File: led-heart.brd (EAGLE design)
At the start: 55 x 44.9 mm, 65 parts, among them IC1 FT232RL, IC2 MSP430F149, Q1 8mhz, T1 MMBT3904, T2 MMBT3904, X1 USB_MINI-B

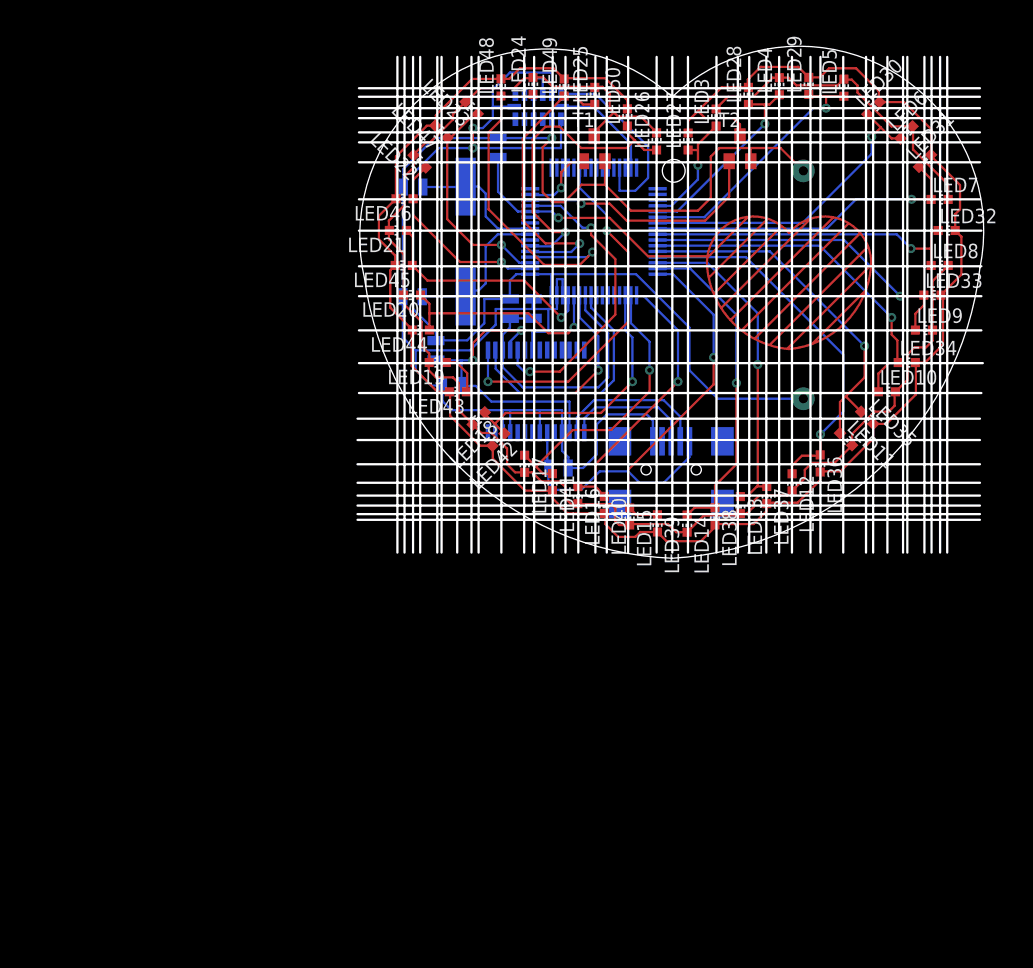
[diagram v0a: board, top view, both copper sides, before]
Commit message: release, fix schematic, pcb, silk, docs
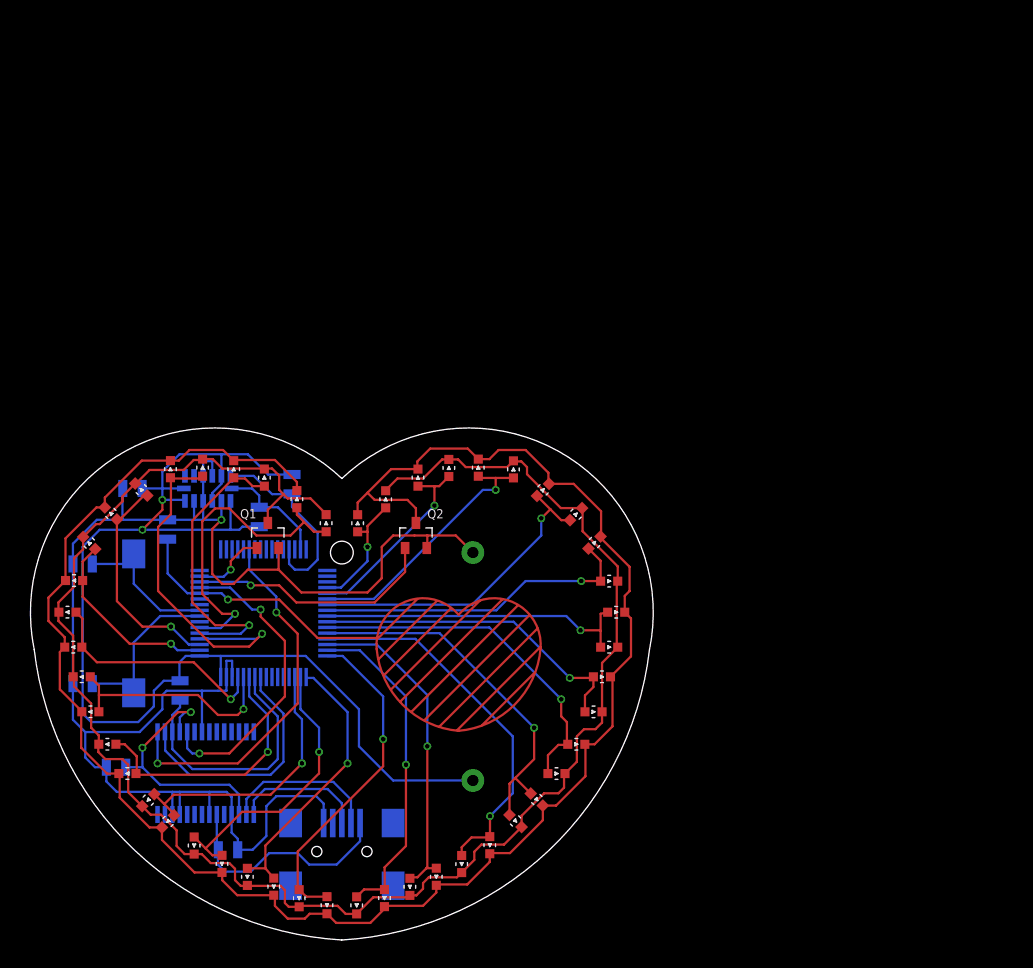
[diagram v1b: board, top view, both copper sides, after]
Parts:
- removed D1: LIS302DL, colibri:LGA14
- removed R5: 100k, colibri:R0805
- removed T1, T2: MMBT3904, transistor:SOT23-BEC
- added IC3: LIS302DL, netcat:LGA14
- added LOGO1: LOGO2, netcat:LOGO2
- added Q2: MMBT3904, netcat:SOT23
- added QZ1: 8MHz, netcat:SM49
- added R2: 4.7k, netcat:R0805
- added R3: 100k, netcat:R0805
- B1: device Di:BATTERY -> netcat:CR2032
- C1, C2: value 0,1u -> 100n; device colibri:C0805 -> netcat:R0805
- C3: value 10n -> 12p; device colibri:C0805 -> netcat:R0805
- C4: device colibri:C0805 -> netcat:R0805
- C5: value 12p -> 100n; device colibri:C0805 -> netcat:R0805
- IC1: device ftdichip:SSOP28 -> netcat:SSOP28
- IC2: value MSP430F149 -> MSP430F249; device texas:SQFP-S-10X10-64 -> netcat:SQFP-S-10X10-64
- LED10, LED11, LED12, LED13, LED14, LED15, LED16, LED17, LED18, LED19, LED20, LED21, LED22, LED23, LED24, LED25, LED26, LED27, LED28, LED29, LED3, LED30, LED31, LED32, LED33, LED34, LED35, LED36, LED37, LED38, LED39, LED4, LED40, LED41, LED42, LED43, LED44, LED45, LED46, LED47, LED48, LED49, LED5, LED50, LED6, LED7, LED8, LED9: device led:CHIP-LED0603 -> netcat:LED0603
- Q1: value 8mhz -> MMBT3904; device crystal:SM49 -> netcat:SOT23
- R1: value 0 -> 4.7k; device colibri:R0805 -> netcat:R0805
- R4: device colibri:R0805 -> netcat:R0805
- U$1: device Di:TOUCH_SENSOR -> netcat:TOUCH_SENSOR
- X1: value USB_MINI-B -> USB-MINI-B; device colibri:USB_MINI-B -> netcat:USB-MINI-B
- moved C3 51.4 mm to (-22.8, -11.5), turned to 180 degrees
- moved C1 44.6 mm to (-19.8, -18.8)
- moved B1 44.3 mm to (11.5, -6.00)
- moved C2 44.3 mm to (-9.99, -26.1)
- moved IC1 44.3 mm to (-11.9, -19.4)
- moved IC2 44.3 mm to (-6.88, -5.32)
- moved LED10 44.3 mm to (18.8, -19.4)
- moved LED11 44.3 mm to (15.2, -23.6)
- moved LED12 44.3 mm to (10.5, -27.3)
- moved LED13 44.3 mm to (5.97, -29.3)
- moved LED14 44.3 mm to (1.30, -31.0)
- moved LED15 44.3 mm to (-3.75, -30.3)
- moved LED16 44.3 mm to (-8.29, -28.5)
- moved LED17 44.3 mm to (-13.0, -25.7)
- moved LED18 44.3 mm to (-17.0, -21.7)
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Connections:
- removed net VCCINT: B1.PLUS, D1.1, D1.12, D1.6, D1.7, IC2.1, IC2.64, R1.1, R4.1
- new net VCC: B1.PLUS, C5.1, IC2.1, IC2.64, IC3.1, IC3.12, IC3.3, IC3.6, IC3.7, R1.1, R2.1, R4.1
- net !BSL_RTS: no longer C3.1
- net EN1: now also Q2.1; no longer T2.B
- net EN2: now also Q1.1; no longer T1.B
- net GND: now also C3.1, C5.2, IC3.10, IC3.11, IC3.2, IC3.4, IC3.5, Q1.2, Q2.2, R3.1; no longer C3.2, C5.1, D1.10, D1.11, D1.2, D1.4, D1.5, R5.1, T1.E, T2.E
- net I2C_SCL: now also IC3.14, R2.2; no longer D1.14, IC2.30
- net I2C_SDA: now also IC3.13, R1.2; no longer D1.13
- net N$10: now also Q2.3; no longer T2.C
- net N$11: now also C4.2, QZ1.1; no longer C5.2, Q1.1
- net N$12: now also R3.2; no longer R5.2
- net N$6: no longer R1.2
- net N$8: now also C3.2, QZ1.2; no longer C4.2, Q1.2
- net N$9: now also Q1.3; no longer T1.C
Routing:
- net VCC: track 0.00 -> 109.2 mm, vias 0 -> 2
- net VCCINT: track 95.4 -> 0.00 mm, vias 2 -> 0
- net N$6: track 26.6 -> 22.5 mm
- net !BSL_RTS: track 25.0 -> 23.0 mm
- net N$8: track 13.6 -> 14.8 mm
- net N$10: track 168.0 -> 168.9 mm
- net GND: track 145.9 -> 145.0 mm
- net N$11: track 12.2 -> 13.0 mm
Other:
- board size 55 x 44.9 mm -> 54.7 x 44.9 mm
- board text added: "github.com/netcatu"
- board text added: "led-heart v1.0.0"

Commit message: new design, qfn packages, buzzer for sound
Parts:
- removed IC3: LIS302DL, netcat:LGA14
- removed R1, R2: 4.7k, netcat:R0805
- removed R3, R4: 100k, netcat:R0805
- added BZ1: (no value), netcat:HYG7525
- added L1: 10uH, netcat:C1812
- added Q3: IRLML2402, netcat:SOT23
- added R5: 100k, netcat:R0402
- added VD1: 4148, netcat:SOD123
- C1: value 100n -> 0.1u; device netcat:R0805 -> netcat:R0402
- C2: value 100n -> 10u; device netcat:R0805 -> netcat:R0603
- C3: value 12p -> 10u; device netcat:R0805 -> netcat:SMC_A
- C4: device netcat:R0805 -> netcat:R0402
- C5: value 100n -> 12p; device netcat:R0805 -> netcat:R0402
- IC1: value FT232RL -> FT232RQ; device netcat:SSOP28 -> netcat:QFN32
- IC2: value MSP430F249 -> MSP430F2370; device netcat:SQFP-S-10X10-64 -> netcat:QFN40-6X6
- Q1, Q2: value MMBT3904 -> IRLML2402
- QZ1: value 8MHz -> 8mhz; device netcat:SM49 -> netcat:3225
- X1: value USB-MINI-B -> USBMICRO_B; device netcat:USB-MINI-B -> netcat:USB_MICROB
- moved LOGO1 29.1 mm to (-17.9, -16.1)
- moved C5 14.2 mm to (-12.4, -7.32), turned to 180 degrees
- moved Q2 13.6 mm to (-6.65, -2.00), flipped to the bottom
- moved C2 12.1 mm to (1.95, -24.1), turned to 90 degrees
- moved C1 10.6 mm to (-11.8, -25.9), turned to 270 degrees
- moved C4 10.5 mm to (-12.4, -2.90), turned to 0 degrees
- moved U$1 10.3 mm to (0.00, -10.3)
- moved IC1 8.57 mm to (-3.80, -22.0), turned to 270 degrees
- moved IC2 6.87 mm to (-8.50, -12.0), turned to 270 degrees
- moved QZ1 6.36 mm to (-12.0, -5.10), turned to 0 degrees
- moved C3 6.18 mm to (-19.8, -6.10), turned to 90 degrees
- moved X1 4.96 mm to (0.00, -31.2)
- moved Q1 1.84 mm to (-4.80, 2.20), flipped to the bottom
- moved B1 0.11 mm to (11.6, -6.10)
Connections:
- removed net BSL_RXD: IC1.5, IC2.13
- removed net BSL_TXD: IC1.1, IC2.22
- removed net I2C_SCL: IC2.31, IC3.14, R2.2
- removed net I2C_SDA: IC2.29, IC3.13, R1.2
- removed net N$1: IC1.15, X1.DP
- removed net N$10: LED27.C, LED28.C, LED29.C, LED30.C, LED31.C, LED32.C, LED33.C, LED34.C, LED35.C, LED36.C, LED37.C, LED38.C, LED39.C, LED40.C, LED41.C, LED42.C, LED43.C, LED44.C, LED45.C, LED46.C, LED47.C, LED48.C, LED49.C, LED50.C, Q2.3
- removed net N$11: C4.2, IC2.9, QZ1.1
- removed net N$12: IC2.12, R3.2, U$1.CON
- removed net N$33: IC1.16, X1.DM
- removed net N$34: C2.1, IC1.20, X1.VBUS
- removed net N$6: C1.1, IC1.17, IC1.4
- removed net N$8: C3.2, IC2.8, QZ1.2
- removed net N$9: LED10.C, LED11.C, LED12.C, LED13.C, LED14.C, LED15.C, LED16.C, LED17.C, LED18.C, LED19.C, LED20.C, LED21.C, LED22.C, LED23.C, LED24.C, LED25.C, LED26.C, LED3.C, LED4.C, LED5.C, LED6.C, LED7.C, LED8.C, LED9.C, Q1.3
- removed net VCC: B1.PLUS, C5.1, IC2.1, IC2.64, IC3.1, IC3.12, IC3.3, IC3.6, IC3.7, R1.1, R2.1, R4.1
- new net 3.3V: B1.PLUS, C3.+, IC2.1, IC2.40, L1.1
- new net 5V: C2.1, IC1.19, X1.VBUS
- new net BOOST: L1.2, VD1.A
- new net LINE1: LED27.C, LED28.C, LED29.C, LED30.C, LED31.C, LED32.C, LED33.C, LED34.C, LED35.C, LED36.C, LED37.C, LED38.C, LED39.C, LED40.C, LED41.C, LED42.C, LED43.C, LED44.C, LED45.C, LED46.C, LED47.C, LED48.C, LED49.C, LED50.C, Q1.3
- new net LINE2: LED10.C, LED11.C, LED12.C, LED13.C, LED14.C, LED15.C, LED16.C, LED17.C, LED18.C, LED19.C, LED20.C, LED21.C, LED22.C, LED23.C, LED24.C, LED25.C, LED26.C, LED3.C, LED4.C, LED5.C, LED6.C, LED7.C, LED8.C, LED9.C, Q3.3
- new net SENS: IC2.8, R5.2, U$1.CON
- new net SENS2: IC2.9, R5.1
- new net SND: IC2.6, Q2.1
- new net USB+DP: IC1.14, X1.D+
- new net USB_DM: IC1.15, X1.D-
- new net VCCIO: C1.1, IC1.1, IC1.16
- new net V_SND: BZ1.1, Q2.3, VD1.C
- new net XIN: C5.2, IC2.2, QZ1.1
- new net XOUT: C4.2, IC2.3, QZ1.3
- net !BSL_DTR: now also IC1.31, IC2.37; no longer IC1.2, IC2.57
- net !BSL_RTS: now also IC1.32, IC2.38; no longer IC1.3, IC2.58, R4.2
- net EN1: now also IC1.2, IC2.5, Q1.1; no longer IC2.14, Q2.1
- net EN2: now also IC2.7, Q3.1; no longer IC2.15, Q1.1
- net GND: now also BZ1.2, C3.-, C5.1, IC1.17, IC1.20, IC1.24, IC1.4, IC2.39, IC2.EXP, Q3.2, QZ1.2, QZ1.4, X1.6, X1.7, X1.8, X1.9; no longer C3.1, C5.2, IC1.18, IC1.21, IC1.25, IC1.7, IC2.62, IC2.63, IC3.10, IC3.11, IC3.2, IC3.4, IC3.5, R3.1
- net LED0: now also IC2.12; no longer IC2.36
- net LED1: now also IC2.13; no longer IC2.37
- net LED10: now also IC2.20; no longer IC2.46
- net LED11: now also IC2.21; no longer IC2.47
- net LED12: now also IC2.22; no longer IC2.48
- net LED13: now also IC2.23; no longer IC2.49
- net LED14: now also IC2.24; no longer IC2.50
- net LED15: now also IC2.25; no longer IC2.51
- net LED16: now also IC2.26; no longer IC2.59
- net LED17: now also IC2.27; no longer IC2.60
- net LED18: now also IC2.28; no longer IC2.61
- net LED19: now also IC2.29; no longer IC2.2
- net LED2: now also IC1.30, IC2.14; no longer IC2.38
- net LED20: now also IC2.30; no longer IC2.3
- net LED21: now also IC2.31; no longer IC2.4
- net LED22: now also IC2.32; no longer IC2.5
- net LED23: now also IC2.33; no longer IC2.6
- net LED3: now also IC2.15; no longer IC2.39
- net LED4: now also IC2.16; no longer IC2.40
- net LED5: now also IC2.17; no longer IC2.41
- net LED6: now also IC2.10; no longer IC2.42
- net LED7: now also IC2.11; no longer IC2.43
- net LED8: now also IC2.18; no longer IC2.44
- net LED9: now also IC2.19; no longer IC2.45
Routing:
- net 3.3V: track 0.00 -> 204.4 mm, vias 0 -> 4
- net N$10: track 168.9 -> 0.00 mm
- net LINE1: track 0.00 -> 164.4 mm, vias 0 -> 1
- net LINE2: track 0.00 -> 160.3 mm, vias 0 -> 1
- net N$9: track 157.5 -> 0.00 mm
- net GND: track 145.0 -> 5.16 mm, vias 1 -> 0
- net VCC: track 109.2 -> 0.00 mm, vias 2 -> 0
- net LED2: track 22.9 -> 107.9 mm, vias 1 -> 3
- net EN1: track 22.0 -> 73.2 mm, vias 1 -> 2
- net LED7: track 31.1 -> 69.6 mm
- net LED6: track 28.9 -> 65.8 mm
- net BSL_TXD: track 32.5 -> 0.00 mm, vias 2 -> 0
- net BSL_RXD: track 27.0 -> 0.00 mm, vias 2 -> 0
- net VCCIO: track 0.00 -> 26.7 mm, vias 0 -> 2
- net N$12: track 23.8 -> 0.00 mm, vias 1 -> 0
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- added copper zone on layer 16, net GND
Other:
- board text added: "led-heart v2.0.0"
- board text removed: "led-heart v1.0.0"
